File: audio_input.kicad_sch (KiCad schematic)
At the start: 46 parts, among them J11 NCJ6FA-H-0, J12 NCJ6FA-H-0, Q2 MMBT3904, Q3 MMBT3904, Q4 MMBT3906, Q5 MMBT3906, U10 THAT1246, U7 OPA1656ID, U8 LM2903, U9 THAT1246

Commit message: final layout
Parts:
- renumbered C37 to C12, C26 to C14, C39 to C17, C36 to C18, C35 to C19, C38 to C20, C33 to C21, C29 to C22, C31 to C23, C28 to C24, C34 to C25, C27 to C26, C41 to C27, C32 to C28, C40 to C29, C43 to C30, C30 to C31, C42 to C32, J11 to J4, J12 to J6, Q2 to Q1, Q4 to Q2, Q5 to Q3, Q3 to Q4, R30 to R1, R27 to R10, R28 to R11, R37 to R12, R34 to R13, R33 to R14, R32 to R15, R24 to R16, R38 to R17, R31 to R18, R36 to R19, R35 to R20, R29 to R3, R25 to R4, R23 to R8, R26 to R9, RV3 to RV7, RV4 to RV8, U9 to U4, U10 to U5, U7 to U6, U8 to U7

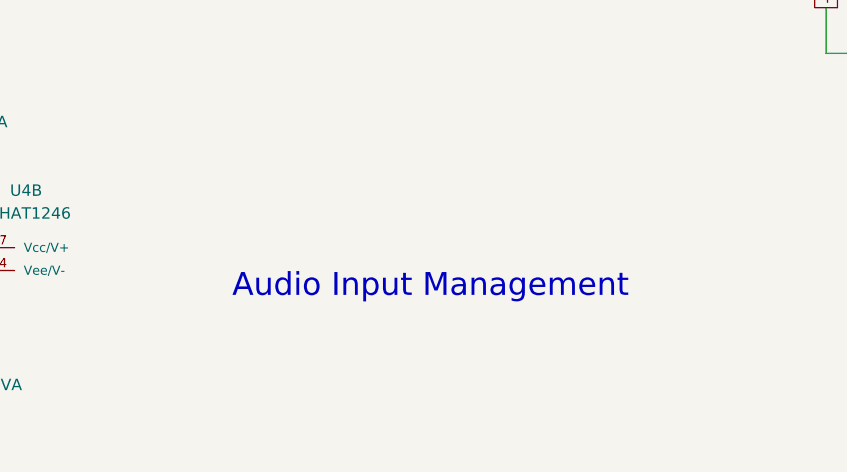
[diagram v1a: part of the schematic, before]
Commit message: added 3d models
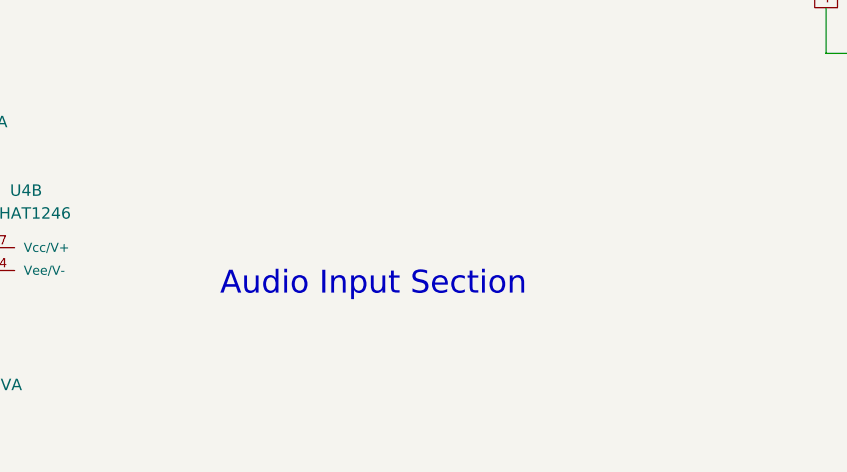
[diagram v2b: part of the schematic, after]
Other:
- note added: "Audio Input Section"
- note removed: "Audio Input Management"
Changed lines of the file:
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@@
 		)
 	)
-	(text "Audio Input Management"
+	(text "Audio Input Section\n"
 		(exclude_from_sim no)
-		(at 185.928 177.038 0)
+		(at 179.578 176.784 0)
 		(effects
 			(font
